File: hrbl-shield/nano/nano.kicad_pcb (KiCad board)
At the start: 2 copper layers, 79.8 x 140.1 mm, 64 parts, among them P1 Digital, P2 Analog, U1 SFH6206-3T, U10 SFH6206-3T, U11 SFH6206-3T, U12 SFH6206-3T, U13 SFH6206-3T, U14 SFH6206-3T, U15 IFX27001TFV50ATMA1CT-ND, U16 SFH6206-3T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

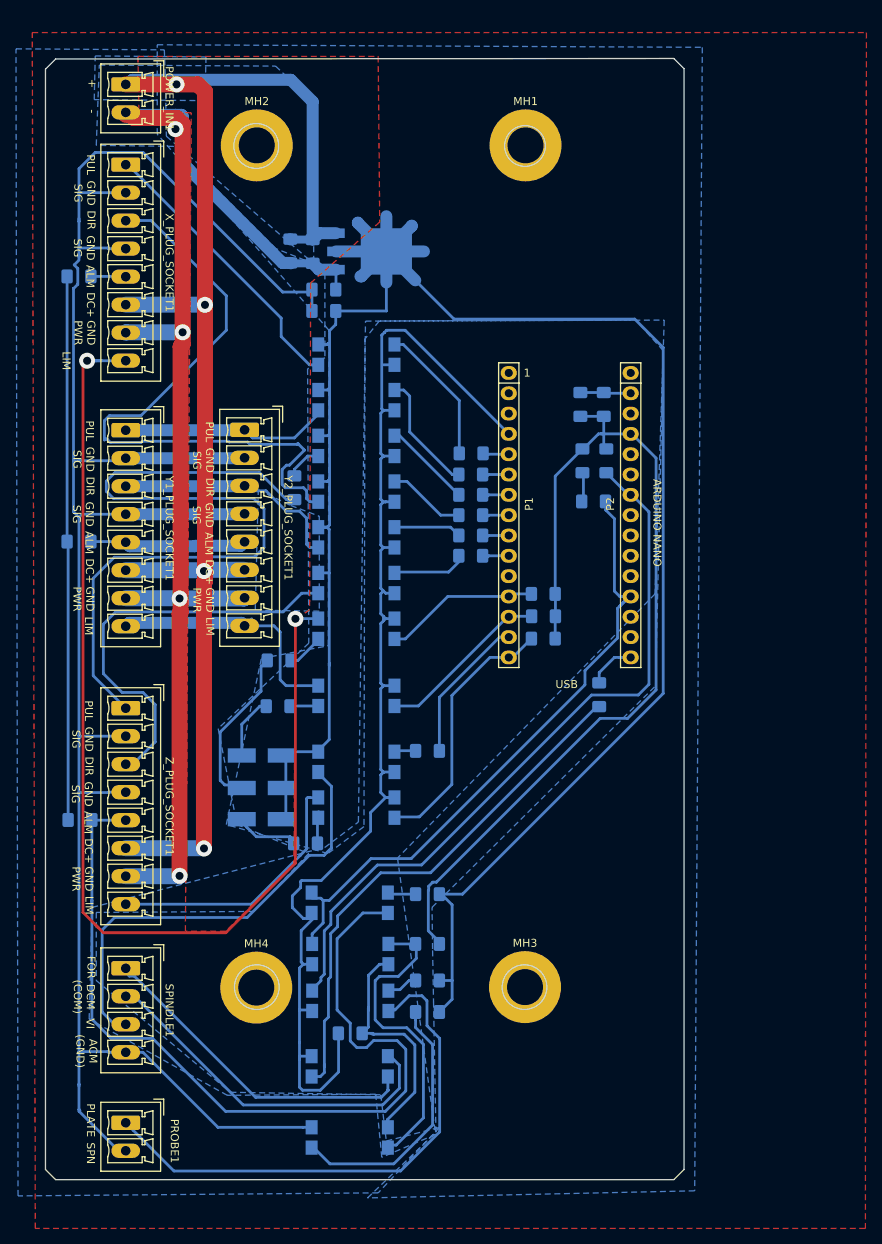
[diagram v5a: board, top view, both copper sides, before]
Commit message: Post for Grbl in fusion360 and nano PCB notes
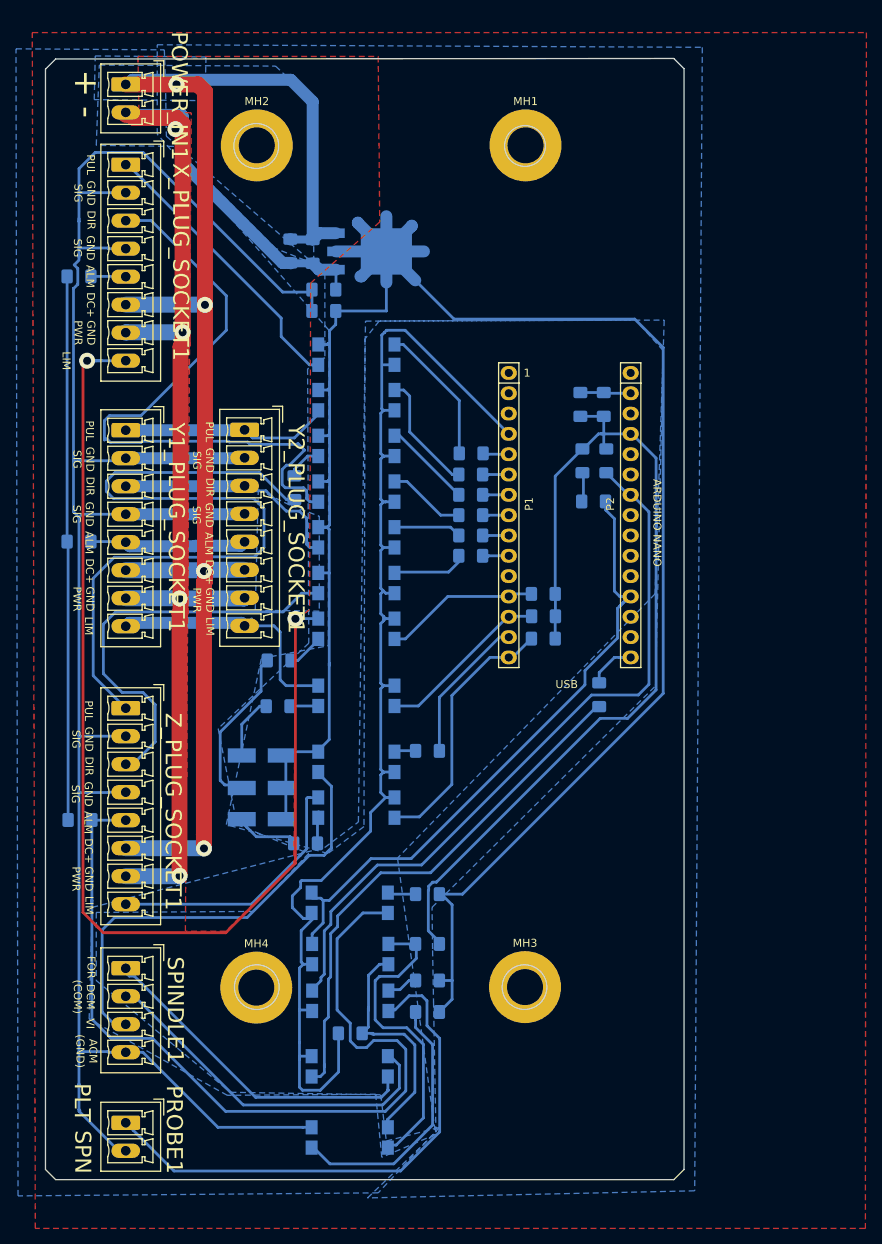
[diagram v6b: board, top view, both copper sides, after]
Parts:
- R23, R24, R25: value 1000 -> 1k
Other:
- board text added: "0"
- board text added: "10uF"
- board text added: "1K"
- board text added: "PLT"
- board text removed: "PLATE"

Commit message: hrbl shield updated and folder cleaned
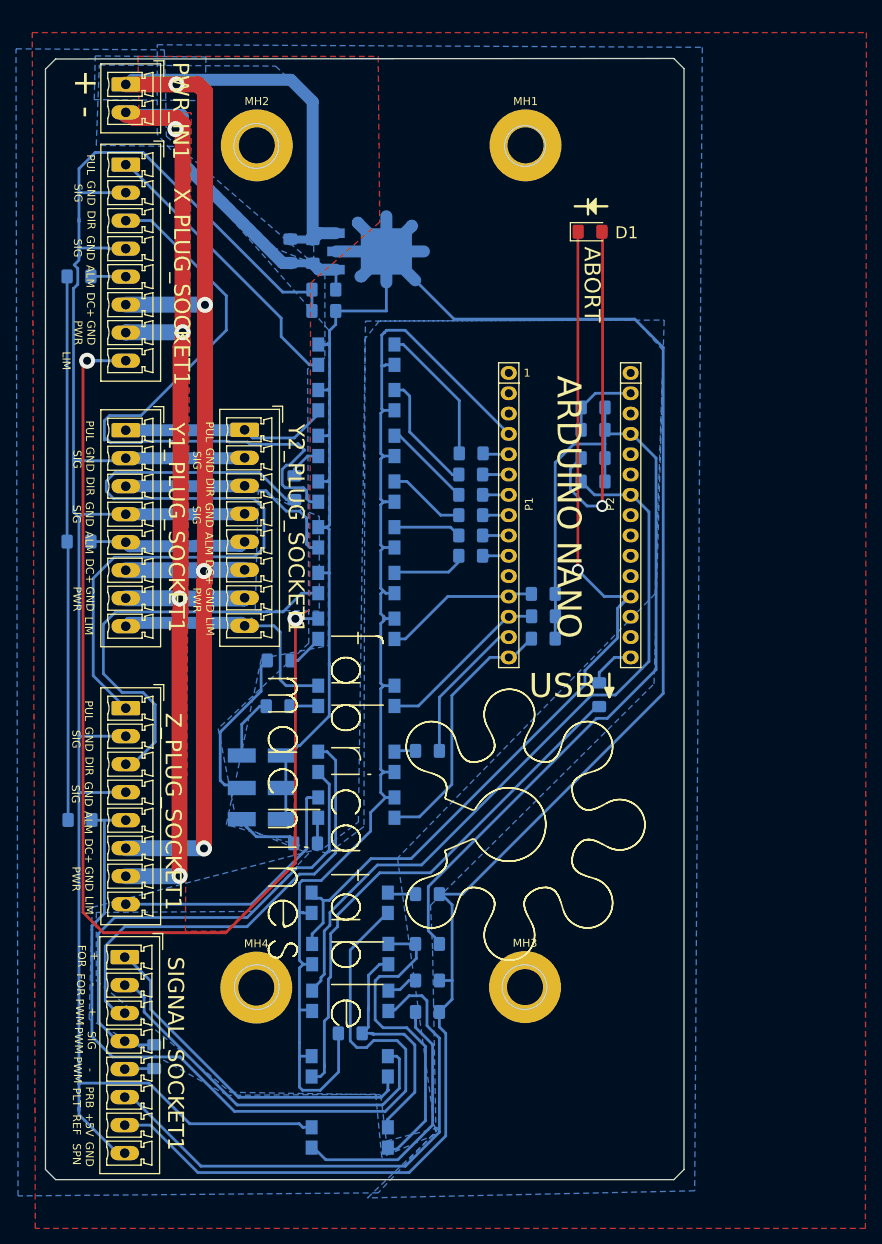
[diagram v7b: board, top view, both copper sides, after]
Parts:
- removed PROBE1: Conn_01x02, Connector_Phoenix_MC:PhoenixContact_MCV_1,5_2-G-3.5_1x02_P3.50mm_Vertical
- removed SPINDLE1: Conn_01x04, Connector_Phoenix_MC:PhoenixContact_MCV_1,5_4-G-3.5_1x04_P3.50mm_Vertical
- added R27: 1000, Resistor_SMD:R_1206_3216Metric_Pad1.42x1.75mm_HandSolder, B.Cu at (95.1, 156.7)
- added REF**: fabricatable_machines, Symbol:Fabricatable_machines_logo, F.Cu at (139.4, 127.6)
- added SIGNAL_SOCKET1: Conn_01x08, Connector_Phoenix_MC:PhoenixContact_MCV_1,5_8-G-3.5_1x08_P3.50mm_Vertical, F.Cu at (91.4, 144.3)
- C3: value 100nF (0.1uF) -> 100nF
- D1: moved to F.Cu
- R23, R24, R25: value 1k -> 1000
- moved D1 33.7 mm to (149.6, 53.6), turned to 0 degrees
- moved C6 3.55 mm to (150.0, 78.4), turned to 0 degrees
- moved R26 3.07 mm to (150.0, 84.8), turned to 180 degrees
- moved C3 1.39 mm to (150.0, 75.6), turned to 0 degrees
- moved R21 1.37 mm to (150.0, 81.9), turned to 0 degrees
- renumbered POWER_IN1 to PWR_IN1
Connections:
- U13 pad 3: /DCM(COM) -> GND_FOR
- U13 pad 4: /FOR -> SOURCE_FOR
- U16 pad 2: /PROBE_PLATE -> PROBE_PLATE
- U7 pad 3: /VI -> SIGNAL_SPEED
- U7 pad 4: 5V_ISO -> SOURCE_SPEED
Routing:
- net PROBE_PLATE: track 0.00 -> 67.5 mm
- net /PROBE_PLATE: track 66.6 -> 0.00 mm
- net SIGNAL_SPEED: track 0.00 -> 63.4 mm
- net 5V_ISO: track 260.2 -> 319.3 mm
- net SOURCE_SPEED: track 0.00 -> 57.7 mm
- net /VI: track 57.0 -> 0.00 mm
- net GND_FOR: track 0.00 -> 47.7 mm
- net /DCM(COM): track 46.0 -> 0.00 mm
- net SOURCE_FOR: track 0.00 -> 44.7 mm
- net /FOR: track 42.4 -> 0.00 mm
- net Net-(D1-Pad2): track 3.53 -> 43.6 mm, vias 0 -> 1
- net ABORT: track 81.4 -> 117.7 mm, vias 0 -> 1
- net GND_SPEED: track 0.00 -> 4.35 mm
- net ALARM_IN: track 201.6 -> 198.6 mm
- net GND: track 193.7 -> 196.6 mm
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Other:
- board text added: "+ FOR"
- board text added: "+ PWM"
- board text added: "+5V REF"
- board text added: "- FOR"
- board text added: "- PWM"
- board text added: "ABORT"
- board text added: "GND SPN"
- board text added: "PRB PLT"
- board text added: "SIG PWM"
- board text removed: "ACM (GND)"
- board text removed: "DCM (COM)"
- board text removed: "FOR"
- board text removed: "PLT"
- board text removed: "SPN"
- board text removed: "VI"
